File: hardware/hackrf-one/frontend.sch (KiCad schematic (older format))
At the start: 139 parts, among them J2 RF-SHIELD-FRAME, J3 RF-SHIELD-COVER, J4 MOUNTING_HOLE, J5 MOUNTING_HOLE, J6 MOUNTING_HOLE, J7 MOUNTING_HOLE, J8 MOUNTING_HOLE, J9 MOUNTING_HOLE, P13 GPO1, P17 GPO6, P19 GPO3, P21 REF_IN, P27 MIXER_SDATA, P31 MIXER_SCLK, P32 MIXER_ENX, P33 MIXER_RESETX, P34 MIX_BYPASS, P35 !MIX_BYPASS, P4 ANTENNA, P42 TX, P43 RX, P44 HP, P45 LP, P46 TX_MIX_BP, P47 RX_MIX_BP, P48 TX_AMP, P49 RX_AMP, P50 AMP_BYPASS, P51 !TX_AMP_PWR, P52 !RX_AMP_PWR, P6 GPO4, P7 GPO2, Q1 MOSFET_P, Q2 MOSFET_P, T1 MIX_IN_BALUN, T2 MIX_OUT_BALUN, U1 SKY13350, U10 SKY13350, U11 SKY13350, U12 SKY13317, U13 MGA-81563, U14 SKY13317, U2 SKY13350, U25 MGA-81563, U3 RX_LOWPASS_FILTER, U4 RFFC5072, U5 SKY13350, U6 SKY13350, U7 SKY13350, U8 RX_HIGHPASS_FILTER, U9 SKY13317

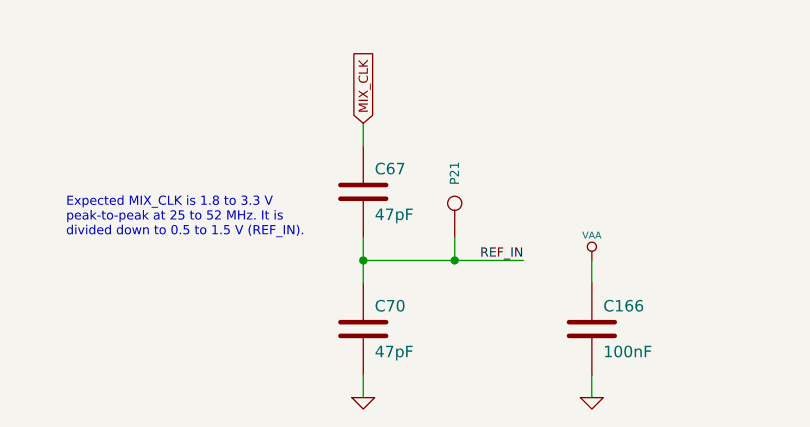
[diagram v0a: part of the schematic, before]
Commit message: improved REF_IN passives
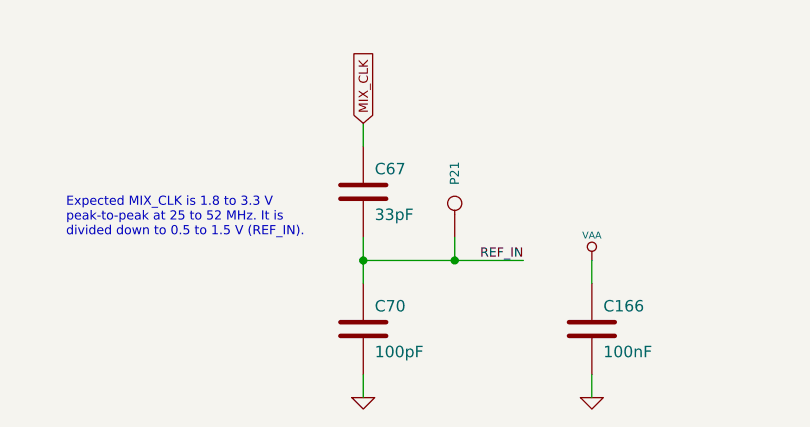
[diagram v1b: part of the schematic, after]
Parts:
- C67: value 47pF -> 33pF; Description CAP CER 47PF 50V 5% NP0 0402 -> CAP CER 33PF 50V 5% NP0 0402; Part Number GRM1555C1H470JZ01D -> GRM1555C1H330JZ01D
- C70: value 47pF -> 100pF; Description CAP CER 47PF 50V 5% NP0 0402 -> CAP CER 100PF 50V 5% NP0 0402; Part Number GRM1555C1H470JZ01D -> GRM1555C1H101JZ01D
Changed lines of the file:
@@
 Expected MIX_CLK is 1.8 to 3.3 V\npeak-to-peak at 25 to 52 MHz. It is\ndivided down to 0.5 to 1.5 V (REF_IN).
-$Comp
-L C C70
-U 1 1 4FB3CC76
-P 6300 10000
-F 0 "C70" H 6350 10100 50  0000 L CNN
-F 1 "47pF" H 6350 9900 50  0000 L CNN
-F 2 "" H 6300 10000 60  0001 C CNN
-F 3 "" H 6300 10000 60  0001 C CNN
-F 4 "Murata" H 6300 9400 60  0001 C CNN "Manufacturer"
-F 5 "GRM1555C1H470JZ01D" H 6300 9400 60  0001 C CNN "Part Number"
-F 6 "CAP CER 47PF 50V 5% NP0 0402" H 6300 9400 60  0001 C CNN "Description"
-	1    6300 10000
-	1    0    0    -1
-$EndComp
 $Comp
 L GND #PWR056
@@
 	1    5400 1850
 	-1   0    0    1
-$EndComp
-$Comp
-L C C67
-U 1 1 4FAECD45
-P 6300 9400
-F 0 "C67" H 6350 9500 50  0000 L CNN
-F 1 "47pF" H 6350 9300 50  0000 L CNN
-F 2 "" H 6300 9400 60  0001 C CNN
-F 3 "" H 6300 9400 60  0001 C CNN
-F 4 "Murata" H 6300 9400 60  0001 C CNN "Manufacturer"
-F 5 "GRM1555C1H470JZ01D" H 6300 9400 60  0001 C CNN "Part Number"
-F 6 "CAP CER 47PF 50V 5% NP0 0402" H 6300 9400 60  0001 C CNN "Description"
-	1    6300 9400
-	1    0    0    -1
 $EndComp
 NoConn ~ 6500 3350
@@
 Text Notes 1200 10300 0    40   ~ 0
 mounting holes are connected to GND
+$Comp
+L C C67
+U 1 1 52901196
+P 6300 9400
+F 0 "C67" H 6350 9500 50  0000 L CNN
+F 1 "33pF" H 6350 9300 50  0000 L CNN
+F 2 "" H 6300 9400 60  0001 C CNN
+F 3 "" H 6300 9400 60  0001 C CNN
+F 4 "Murata" H 17650 11650 60  0001 C CNN "Manufacturer"
+F 5 "GRM1555C1H330JZ01D" H 17650 11650 60  0001 C CNN "Part Number"
+F 6 "CAP CER 33PF 50V 5% NP0 0402" H 17650 11650 60  0001 C CNN "Description"
+	1    6300 9400
+	1    0    0    -1
+$EndComp
+$Comp
+L C C70
+U 1 1 529011D6
+P 6300 10000
+F 0 "C70" H 6350 10100 50  0000 L CNN
+F 1 "100pF" H 6350 9900 50  0000 L CNN
+F 2 "" H 6300 10000 60  0001 C CNN
+F 3 "" H 6300 10000 60  0001 C CNN
+F 4 "Murata" H 9300 11550 60  0001 C CNN "Manufacturer"
+F 5 "GRM1555C1H101JZ01D" H 9300 11550 60  0001 C CNN "Part Number"
+F 6 "CAP CER 100PF 50V 5% NP0 0402" H 9300 11550 60  0001 C CNN "Description"
+	1    6300 10000
+	1    0    0    -1
+$EndComp
 $EndSCHEMATC

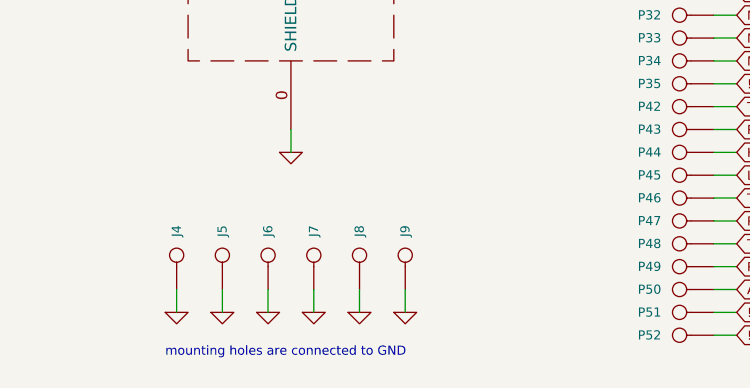
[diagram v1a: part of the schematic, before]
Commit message: clippable GND test point
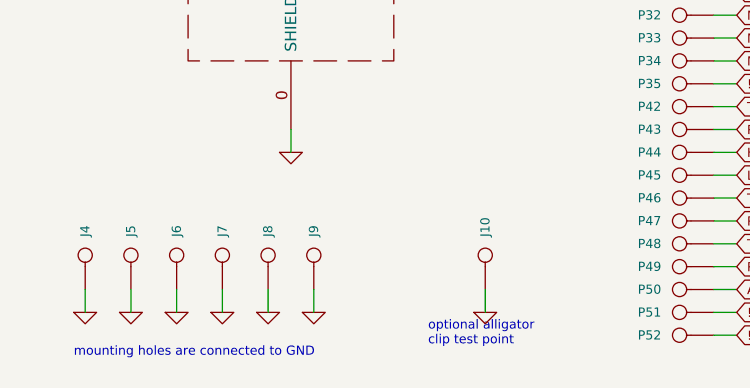
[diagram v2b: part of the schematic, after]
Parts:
- added J10: GND_CLIP, symbol CONN_1
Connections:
- net GND: now also J10.1
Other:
- note added: "optional alligator\nclip test point"
- moved on the sheet: J4, J5, J6, J7, J8, J9

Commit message: analog baseband header consolidation
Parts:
- J10: Description (none) -> PC TEST POINT TIN SMD; Manufacturer (none) -> Harwin; Part Number (none) -> S1751-46R
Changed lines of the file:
@@
 Sheet 2 4
 Title "HackRF One frontend"
-Date "25 nov 2013"
+Date "27 nov 2013"
 Rev ""
 Comp "Copyright 2012 Michael Ossmann"
@@
 F 2 "" H 2600 9850 60  0001 C CNN
 F 3 "" H 2600 9850 60  0001 C CNN
-F 4 "DNP" H 2600 9850 60  0001 C CNN "Note"
+F 4 "Harwin" H 2600 9850 60  0001 C CNN "Manufacturer"
+F 5 "S1751-46R" H 2600 9850 60  0001 C CNN "Part Number"
+F 6 "PC TEST POINT TIN SMD" H 2600 9850 60  0001 C CNN "Description"
+F 7 "DNP" H 2600 9850 60  0001 C CNN "Note"
 	1    2600 9850
 	0    -1   -1   0

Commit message: replaced obsolete capacitor selections
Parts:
- C1, C10, C11, C16, C19, C22, C24, C29, C3, C30, C33, C34, C35, C36, C37, C38, C39, C40, C45, C47, C5, C54, C55, C56, C57, C60, C63, C65, C66, C67, C7: Part Number GRM1555C1H330JZ01D -> GRM1555C1H330JA01D
- C160, C41, C42, C52, C70: Part Number GRM1555C1H101JZ01D -> GRM1555C1H101JA01D
- C21, C26, C27, C32, C43, C48, C51, C8: Part Number GRM1555C1H470JZ01D -> GRM1555C1H470JA01D

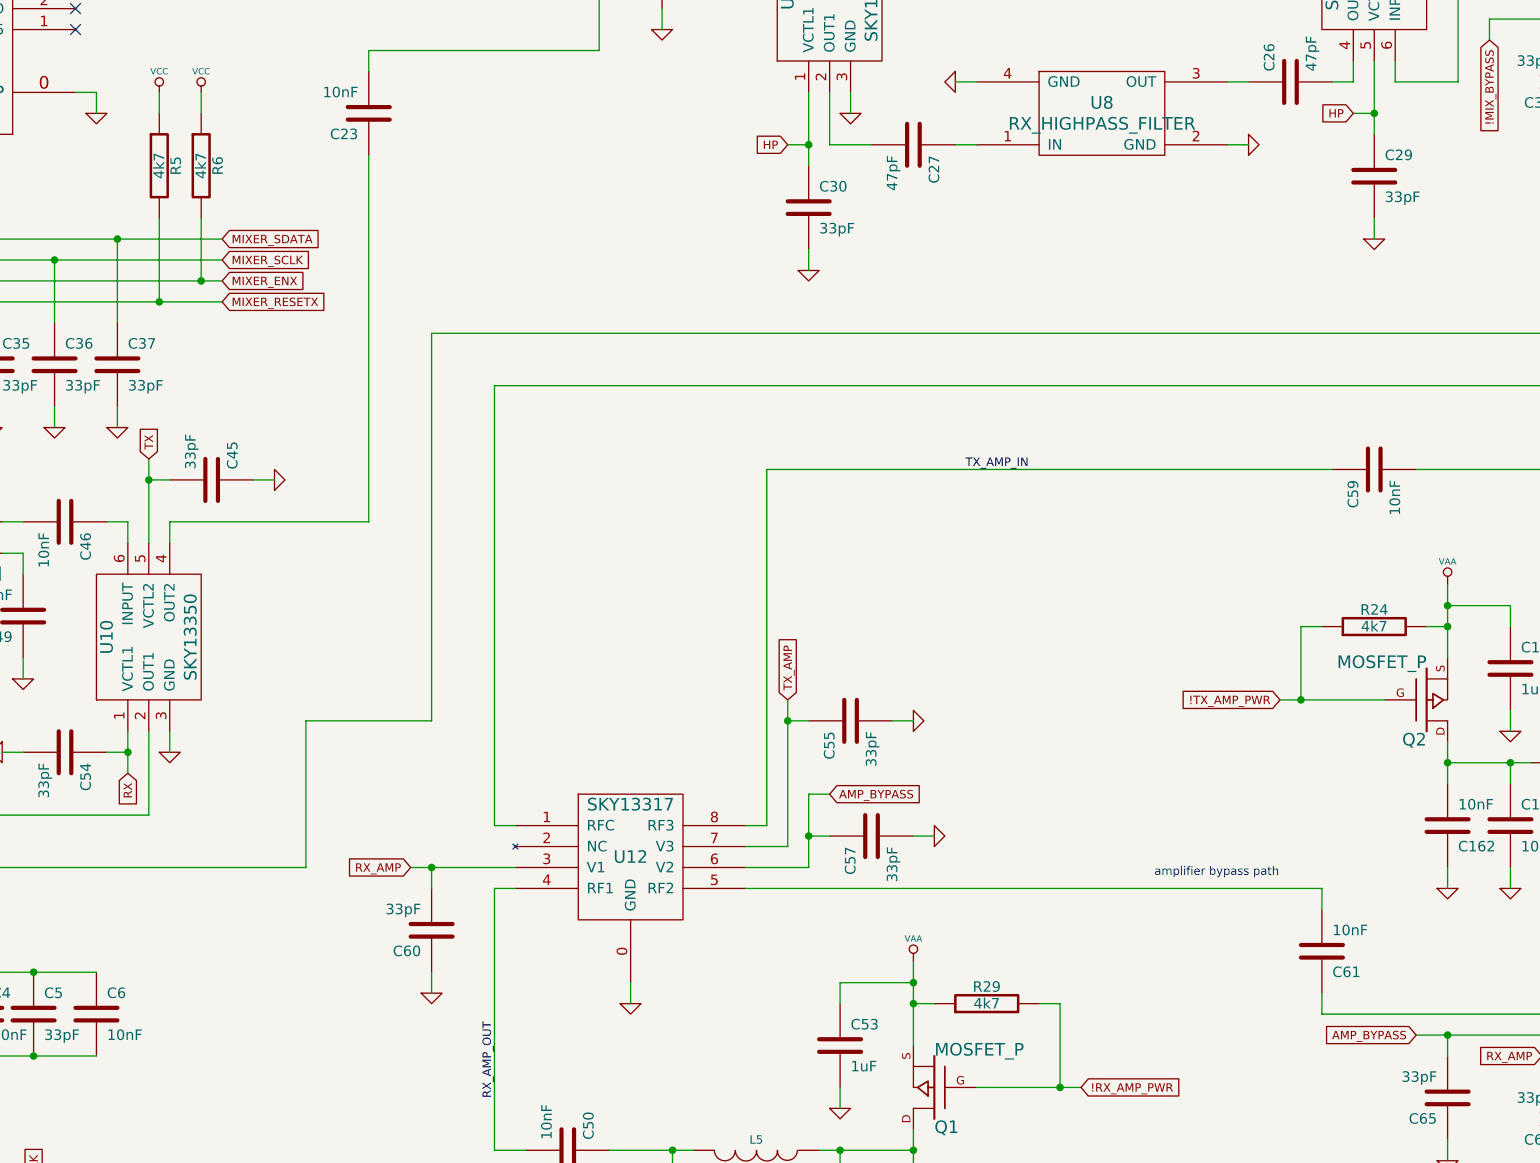
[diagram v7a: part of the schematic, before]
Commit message: changed some 4k7 pull-up or pull-down resistors to 10k to reduce BOM
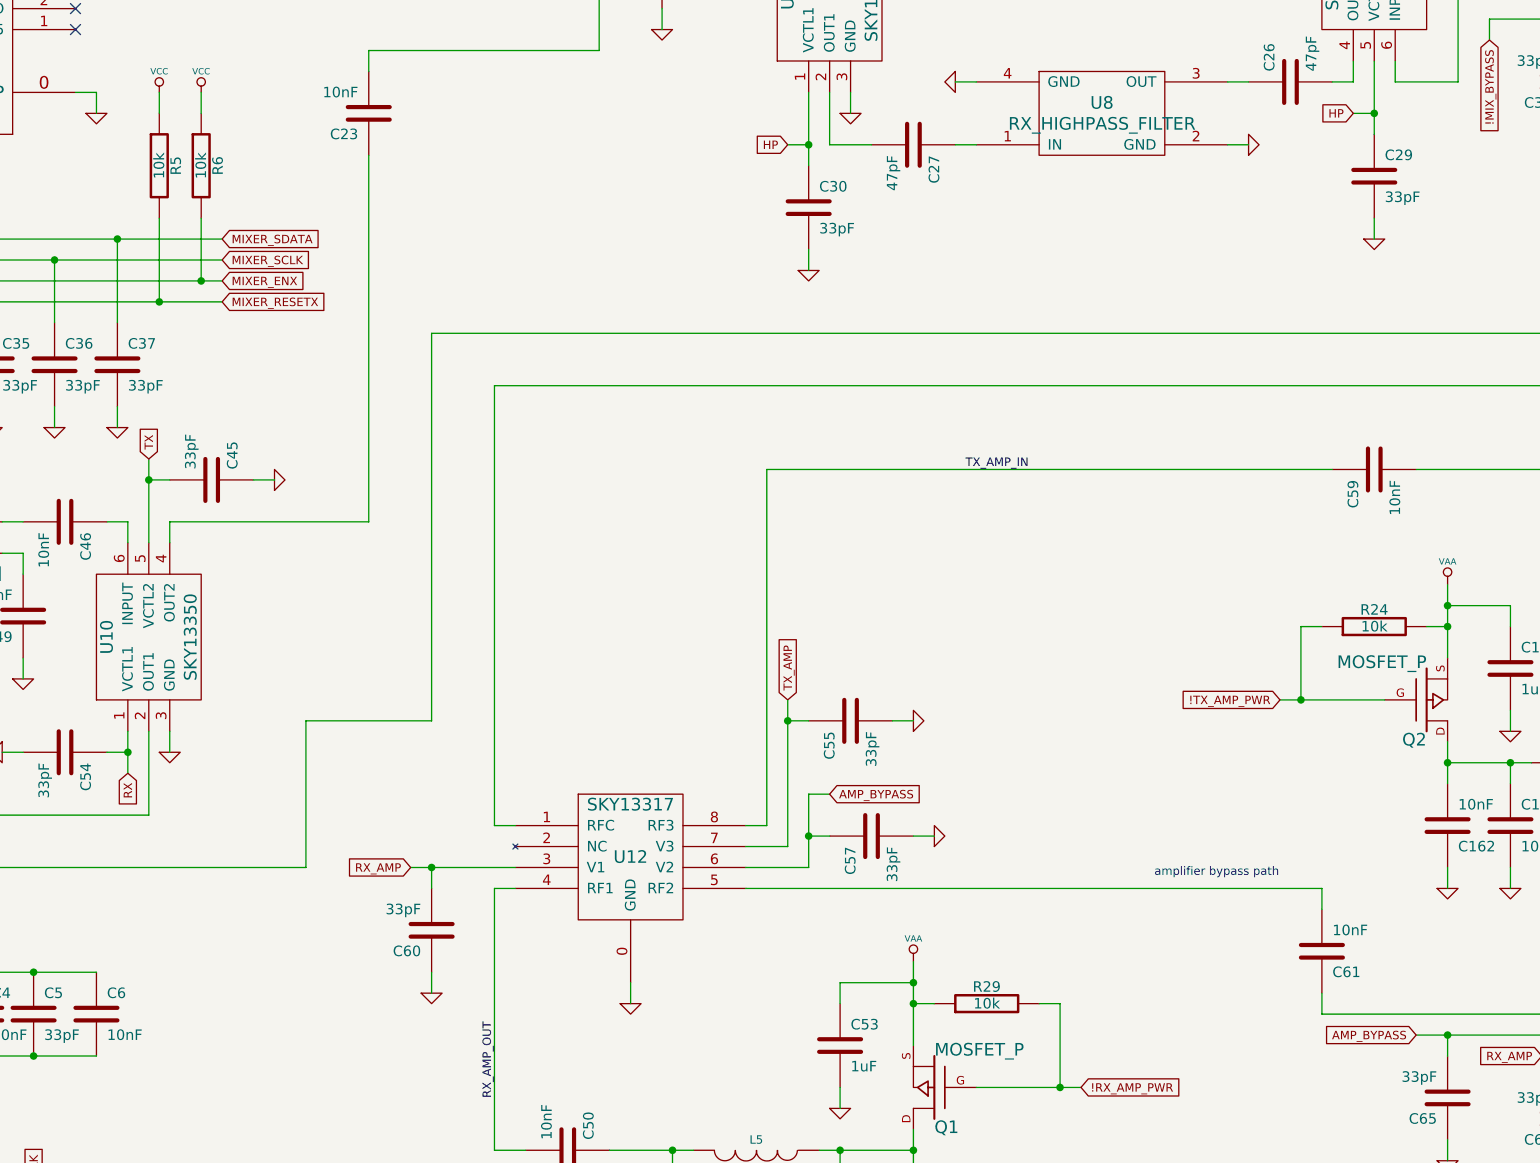
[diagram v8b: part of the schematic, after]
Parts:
- R24, R29, R5, R6: value 4k7 -> 10k; Description RES 4.7K OHM 1/16W 5% 0402 SMD -> RES 10K OHM 1/16W 5% 0402 SMD; Part Number RMCF0402JT4K70 -> RMCF0402JT10K0
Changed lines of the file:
@@
 P 12700 6300
 F 0 "R24" V 12780 6300 50  0000 C CNN
-F 1 "4k7" V 12700 6300 50  0000 C CNN
+F 1 "10k" V 12700 6300 50  0000 C CNN
 F 2 "" H 12700 6300 60  0001 C CNN
 F 3 "" H 12700 6300 60  0001 C CNN
 F 4 "Stackpole" H 12700 6300 60  0001 C CNN "Manufacturer"
-F 5 "RMCF0402JT4K70" H 12700 6300 60  0001 C CNN "Part Number"
-F 6 "RES 4.7K OHM 1/16W 5% 0402 SMD" H 12700 6300 60  0001 C CNN "Description"
+F 5 "RMCF0402JT10K0" H 12700 6300 60  0001 C CNN "Part Number"
+F 6 "RES 10K OHM 1/16W 5% 0402 SMD" H 12700 6300 60  0001 C CNN "Description"
 	1    12700 6300
 	0    -1   -1   0
@@
 P 10850 8100
 F 0 "R29" V 10930 8100 50  0000 C CNN
-F 1 "4k7" V 10850 8100 50  0000 C CNN
+F 1 "10k" V 10850 8100 50  0000 C CNN
 F 2 "" H 10850 8100 60  0001 C CNN
 F 3 "" H 10850 8100 60  0001 C CNN
 F 4 "Stackpole" H 10850 8100 60  0001 C CNN "Manufacturer"
-F 5 "RMCF0402JT4K70" H 10850 8100 60  0001 C CNN "Part Number"
-F 6 "RES 4.7K OHM 1/16W 5% 0402 SMD" H 10850 8100 60  0001 C CNN "Description"
+F 5 "RMCF0402JT10K0" H 10850 8100 60  0001 C CNN "Part Number"
+F 6 "RES 10K OHM 1/16W 5% 0402 SMD" H 10850 8100 60  0001 C CNN "Description"
 	1    10850 8100
 	0    -1   -1   0
@@
 P 7100 4100
 F 0 "R6" V 7180 4100 50  0000 C CNN
-F 1 "4k7" V 7100 4100 50  0000 C CNN
+F 1 "10k" V 7100 4100 50  0000 C CNN
 F 2 "" H 7100 4100 60  0001 C CNN
 F 3 "" H 7100 4100 60  0001 C CNN
 F 4 "Stackpole" H 7100 4100 60  0001 C CNN "Manufacturer"
-F 5 "RMCF0402JT4K70" H 7100 4100 60  0001 C CNN "Part Number"
-F 6 "RES 4.7K OHM 1/16W 5% 0402 SMD" H 7100 4100 60  0001 C CNN "Description"
+F 5 "RMCF0402JT10K0" H 7100 4100 60  0001 C CNN "Part Number"
+F 6 "RES 10K OHM 1/16W 5% 0402 SMD" H 7100 4100 60  0001 C CNN "Description"
 	1    7100 4100
 	1    0    0    -1
@@
 P 6900 4100
 F 0 "R5" V 6980 4100 50  0000 C CNN
-F 1 "4k7" V 6900 4100 50  0000 C CNN
+F 1 "10k" V 6900 4100 50  0000 C CNN
 F 2 "" H 6900 4100 60  0001 C CNN
 F 3 "" H 6900 4100 60  0001 C CNN
 F 4 "Stackpole" H 6900 4100 60  0001 C CNN "Manufacturer"
-F 5 "RMCF0402JT4K70" H 6900 4100 60  0001 C CNN "Part Number"
-F 6 "RES 4.7K OHM 1/16W 5% 0402 SMD" H 6900 4100 60  0001 C CNN "Description"
+F 5 "RMCF0402JT10K0" H 6900 4100 60  0001 C CNN "Part Number"
+F 6 "RES 10K OHM 1/16W 5% 0402 SMD" H 6900 4100 60  0001 C CNN "Description"
 	1    6900 4100
 	1    0    0    -1
